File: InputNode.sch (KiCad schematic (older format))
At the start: 3 parts, among them J6 Conn_01x04_Female

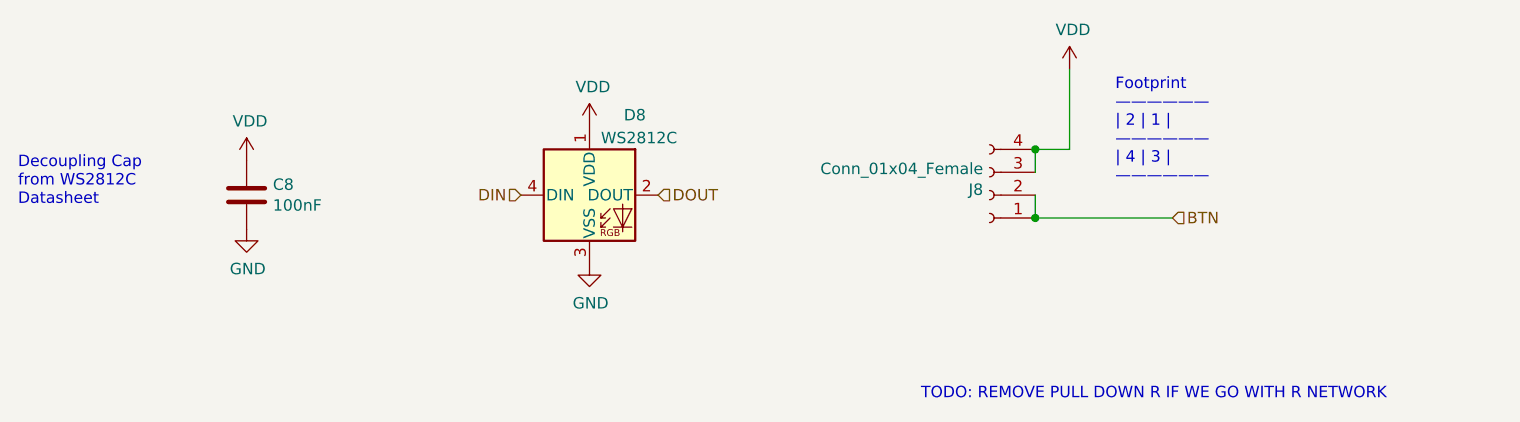
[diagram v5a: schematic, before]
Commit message: finished first pass at routing
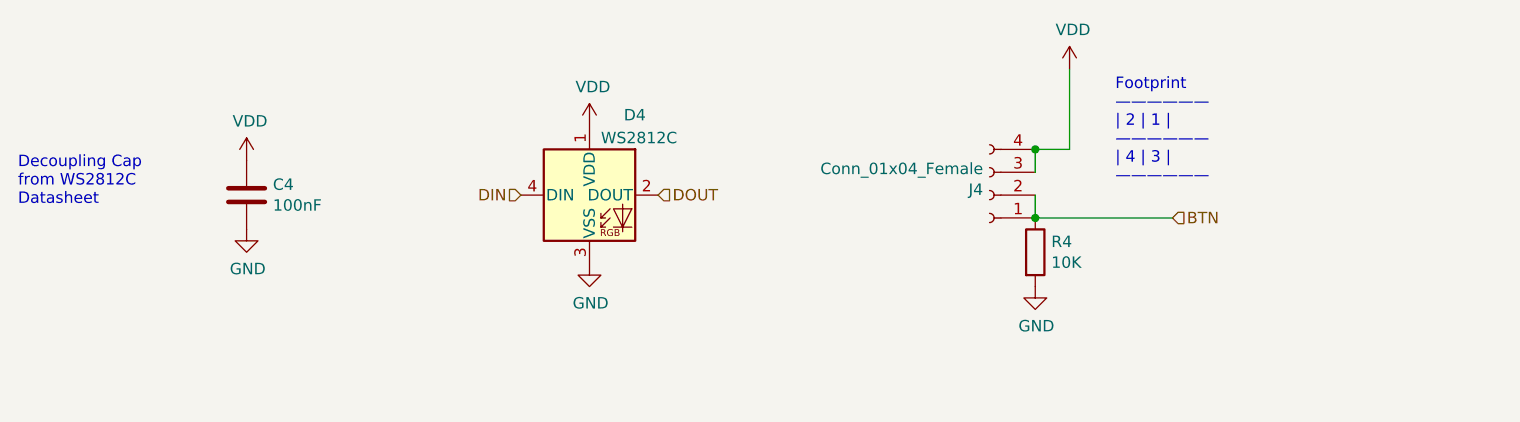
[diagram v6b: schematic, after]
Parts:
- added R1: 10K, Resistor_SMD:R_0805_2012Metric_Pad1.20x1.40mm_HandSolder, symbol Device:R
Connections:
- net BTN: now also R1.1
- net GND: now also R1.2
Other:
- note removed: "TODO: REMOVE PULL DOWN R IF WE GO WITH R NETWORK"
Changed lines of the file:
@@
 $Descr A4 11693 8268
 encoding utf-8
-Sheet 9 9
+Sheet 5 9
 Title ""
 Date ""
@@
 AR Path="/61554F98/61493950" Ref="#PWR049"  Part="1"
 AR Path="/61555D68/61493950" Ref="#PWR?"  Part="1"
-F 0 "#PWR049" H 7700 3100 50  0001 C CNN
+F 0 "#PWR025" H 7700 3100 50  0001 C CNN
 F 1 "VDD" H 7715 3423 50  0000 C CNN
 F 2 "" H 7700 3250 50  0001 C CNN
@@
 AR Path="/61554F98/61493958" Ref="D8"  Part="1"
 AR Path="/61555D68/61493958" Ref="D?"  Part="1"
-F 0 "D8" H 5750 4150 50  0000 L CNN
+F 0 "D4" H 5750 4150 50  0000 L CNN
 F 1 "WS2812C" H 5650 4050 50  0000 L CNN
 F 2 "LED_SMD:LED_WS2812B_PLCC4_5.0x5.0mm_P3.2mm" H 5650 3500 50  0001 L TNN
@@
 AR Path="/61554F98/61495684" Ref="#PWR048"  Part="1"
 AR Path="/61555D68/61495684" Ref="#PWR?"  Part="1"
-F 0 "#PWR048" H 5600 3850 50  0001 C CNN
+F 0 "#PWR024" H 5600 3850 50  0001 C CNN
 F 1 "GND" H 5605 3927 50  0000 C CNN
 F 2 "" H 5600 4100 50  0001 C CNN
@@
 AR Path="/61554F98/61495D51" Ref="#PWR047"  Part="1"
 AR Path="/61555D68/61495D51" Ref="#PWR?"  Part="1"
-F 0 "#PWR047" H 5600 3350 50  0001 C CNN
+F 0 "#PWR023" H 5600 3350 50  0001 C CNN
 F 1 "VDD" H 5615 3673 50  0000 C CNN
 F 2 "" H 5600 3500 50  0001 C CNN
@@
 AR Path="/61554F98/614A34FE" Ref="C8"  Part="1"
 AR Path="/61555D68/614A34FE" Ref="C?"  Part="1"
-F 0 "C8" H 4215 3846 50  0000 L CNN
+F 0 "C4" H 4215 3846 50  0000 L CNN
 F 1 "100nF" H 4215 3755 50  0000 L CNN
 F 2 "Capacitor_SMD:C_0805_2012Metric_Pad1.15x1.40mm_HandSolder" H 4138 3650 50  0001 C CNN
@@
 AR Path="/61554F98/614A4287" Ref="#PWR046"  Part="1"
 AR Path="/61555D68/614A4287" Ref="#PWR?"  Part="1"
-F 0 "#PWR046" H 4100 3700 50  0001 C CNN
+F 0 "#PWR022" H 4100 3700 50  0001 C CNN
 F 1 "GND" H 4105 3777 50  0000 C CNN
 F 2 "" H 4100 3950 50  0001 C CNN
@@
 AR Path="/61554F98/614A4795" Ref="#PWR045"  Part="1"
 AR Path="/61555D68/614A4795" Ref="#PWR?"  Part="1"
-F 0 "#PWR045" H 4100 3500 50  0001 C CNN
+F 0 "#PWR021" H 4100 3500 50  0001 C CNN
 F 1 "VDD" H 4115 3823 50  0000 C CNN
 F 2 "" H 4100 3650 50  0001 C CNN
@@
 AR Path="/61554F92/6156DDAC" Ref="J7"  Part="1"
 AR Path="/61554F98/6156DDAC" Ref="J8"  Part="1"
-F 0 "J8" H 7378 3776 50  0000 L CNN
+F 0 "J4" H 7378 3776 50  0000 L CNN
 F 1 "Conn_01x04_Female" H 7378 3685 50  0000 L CNN
 F 2 "Connector_PinSocket_2.54mm:PinSocket_2x02_P2.54mm_Vertical" H 7350 3800 50  0001 C CNN
@@
 Connection ~ 7550 3600
 Connection ~ 7550 3900
-Text Notes 7050 4700 0    50   ~ 0
-TODO: REMOVE PULL DOWN R IF WE GO WITH R NETWORK
 Wire Wire Line
 	7550 3900 8150 3900
+$Comp
+L Device:R R1
+U 1 1 6160802E
+P 7550 4050
+AR Path="/6149038E/6160802E" Ref="R1"  Part="1"
+AR Path="/61554F98/6160802E" Ref="R8"  Part="1"
+AR Path="/614A08BA/6160802E" Ref="R2"  Part="1"
+AR Path="/61551931/6160802E" Ref="R3"  Part="1"
+AR Path="/6155214B/6160802E" Ref="R4"  Part="1"
+AR Path="/61552612/6160802E" Ref="R5"  Part="1"
+AR Path="/61552B2D/6160802E" Ref="R6"  Part="1"
+AR Path="/61554F92/6160802E" Ref="R7"  Part="1"
+F 0 "R4" H 7620 4096 50  0000 L CNN
+F 1 "10K" H 7620 4005 50  0000 L CNN
+F 2 "Resistor_SMD:R_0805_2012Metric_Pad1.20x1.40mm_HandSolder" V 7480 4050 50  0001 C CNN
+F 3 "~" H 7550 4050 50  0001 C CNN
+	1    7550 4050
+	1    0    0    -1
+$EndComp
+$Comp
+L power:GND #PWR?
+U 1 1 61608726
+P 7550 4200
+AR Path="/61608726" Ref="#PWR?"  Part="1"
+AR Path="/6149038E/61608726" Ref="#PWR0103"  Part="1"
+AR Path="/614A08BA/61608726" Ref="#PWR0104"  Part="1"
+AR Path="/61551931/61608726" Ref="#PWR0105"  Part="1"
+AR Path="/6155214B/61608726" Ref="#PWR0106"  Part="1"
+AR Path="/61552612/61608726" Ref="#PWR0107"  Part="1"
+AR Path="/61552B2D/61608726" Ref="#PWR0108"  Part="1"
+AR Path="/61553054/61608726" Ref="#PWR?"  Part="1"
+AR Path="/61554F92/61608726" Ref="#PWR0109"  Part="1"
+AR Path="/61554F98/61608726" Ref="#PWR0110"  Part="1"
+AR Path="/61555D68/61608726" Ref="#PWR?"  Part="1"
+F 0 "#PWR0106" H 7550 3950 50  0001 C CNN
+F 1 "GND" H 7555 4027 50  0000 C CNN
+F 2 "" H 7550 4200 50  0001 C CNN
+F 3 "" H 7550 4200 50  0001 C CNN
+	1    7550 4200
+	1    0    0    -1
+$EndComp
 $EndSCHEMATC

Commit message: updated with todo for routing around screws
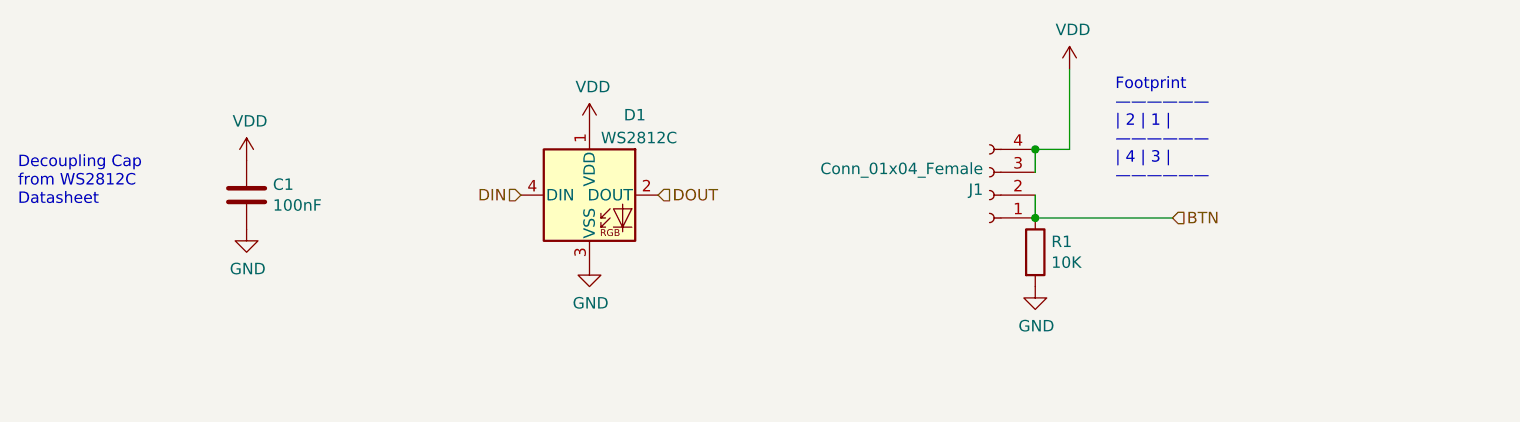
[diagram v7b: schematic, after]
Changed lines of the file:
@@
 $Descr A4 11693 8268
 encoding utf-8
-Sheet 5 9
+Sheet 2 9
 Title ""
 Date ""
@@
 AR Path="/61554F98/61493950" Ref="#PWR049"  Part="1"
 AR Path="/61555D68/61493950" Ref="#PWR?"  Part="1"
-F 0 "#PWR025" H 7700 3100 50  0001 C CNN
+F 0 "#PWR05" H 7700 3100 50  0001 C CNN
 F 1 "VDD" H 7715 3423 50  0000 C CNN
 F 2 "" H 7700 3250 50  0001 C CNN
@@
 AR Path="/61554F98/61493958" Ref="D8"  Part="1"
 AR Path="/61555D68/61493958" Ref="D?"  Part="1"
-F 0 "D4" H 5750 4150 50  0000 L CNN
+F 0 "D1" H 5750 4150 50  0000 L CNN
 F 1 "WS2812C" H 5650 4050 50  0000 L CNN
 F 2 "LED_SMD:LED_WS2812B_PLCC4_5.0x5.0mm_P3.2mm" H 5650 3500 50  0001 L TNN
@@
 AR Path="/61554F98/61495684" Ref="#PWR048"  Part="1"
 AR Path="/61555D68/61495684" Ref="#PWR?"  Part="1"
-F 0 "#PWR024" H 5600 3850 50  0001 C CNN
+F 0 "#PWR04" H 5600 3850 50  0001 C CNN
 F 1 "GND" H 5605 3927 50  0000 C CNN
 F 2 "" H 5600 4100 50  0001 C CNN
@@
 AR Path="/61554F98/61495D51" Ref="#PWR047"  Part="1"
 AR Path="/61555D68/61495D51" Ref="#PWR?"  Part="1"
-F 0 "#PWR023" H 5600 3350 50  0001 C CNN
+F 0 "#PWR03" H 5600 3350 50  0001 C CNN
 F 1 "VDD" H 5615 3673 50  0000 C CNN
 F 2 "" H 5600 3500 50  0001 C CNN
@@
 AR Path="/61554F98/614A34FE" Ref="C8"  Part="1"
 AR Path="/61555D68/614A34FE" Ref="C?"  Part="1"
-F 0 "C4" H 4215 3846 50  0000 L CNN
+F 0 "C1" H 4215 3846 50  0000 L CNN
 F 1 "100nF" H 4215 3755 50  0000 L CNN
 F 2 "Capacitor_SMD:C_0805_2012Metric_Pad1.15x1.40mm_HandSolder" H 4138 3650 50  0001 C CNN
@@
 AR Path="/61554F98/614A4287" Ref="#PWR046"  Part="1"
 AR Path="/61555D68/614A4287" Ref="#PWR?"  Part="1"
-F 0 "#PWR022" H 4100 3700 50  0001 C CNN
+F 0 "#PWR08" H 4100 3700 50  0001 C CNN
 F 1 "GND" H 4105 3777 50  0000 C CNN
 F 2 "" H 4100 3950 50  0001 C CNN
@@
 AR Path="/61554F98/614A4795" Ref="#PWR045"  Part="1"
 AR Path="/61555D68/614A4795" Ref="#PWR?"  Part="1"
-F 0 "#PWR021" H 4100 3500 50  0001 C CNN
+F 0 "#PWR07" H 4100 3500 50  0001 C CNN
 F 1 "VDD" H 4115 3823 50  0000 C CNN
 F 2 "" H 4100 3650 50  0001 C CNN
@@
 AR Path="/61554F92/6156DDAC" Ref="J7"  Part="1"
 AR Path="/61554F98/6156DDAC" Ref="J8"  Part="1"
-F 0 "J4" H 7378 3776 50  0000 L CNN
+F 0 "J1" H 7378 3776 50  0000 L CNN
 F 1 "Conn_01x04_Female" H 7378 3685 50  0000 L CNN
 F 2 "Connector_PinSocket_2.54mm:PinSocket_2x02_P2.54mm_Vertical" H 7350 3800 50  0001 C CNN
@@
 AR Path="/61552B2D/6160802E" Ref="R6"  Part="1"
 AR Path="/61554F92/6160802E" Ref="R7"  Part="1"
-F 0 "R4" H 7620 4096 50  0000 L CNN
+F 0 "R1" H 7620 4096 50  0000 L CNN
 F 1 "10K" H 7620 4005 50  0000 L CNN
 F 2 "Resistor_SMD:R_0805_2012Metric_Pad1.20x1.40mm_HandSolder" V 7480 4050 50  0001 C CNN
@@
 AR Path="/61554F98/61608726" Ref="#PWR0110"  Part="1"
 AR Path="/61555D68/61608726" Ref="#PWR?"  Part="1"
-F 0 "#PWR0106" H 7550 3950 50  0001 C CNN
+F 0 "#PWR0103" H 7550 3950 50  0001 C CNN
 F 1 "GND" H 7555 4027 50  0000 C CNN
 F 2 "" H 7550 4200 50  0001 C CNN

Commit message: fixed added cap for mux and fixed drc errors
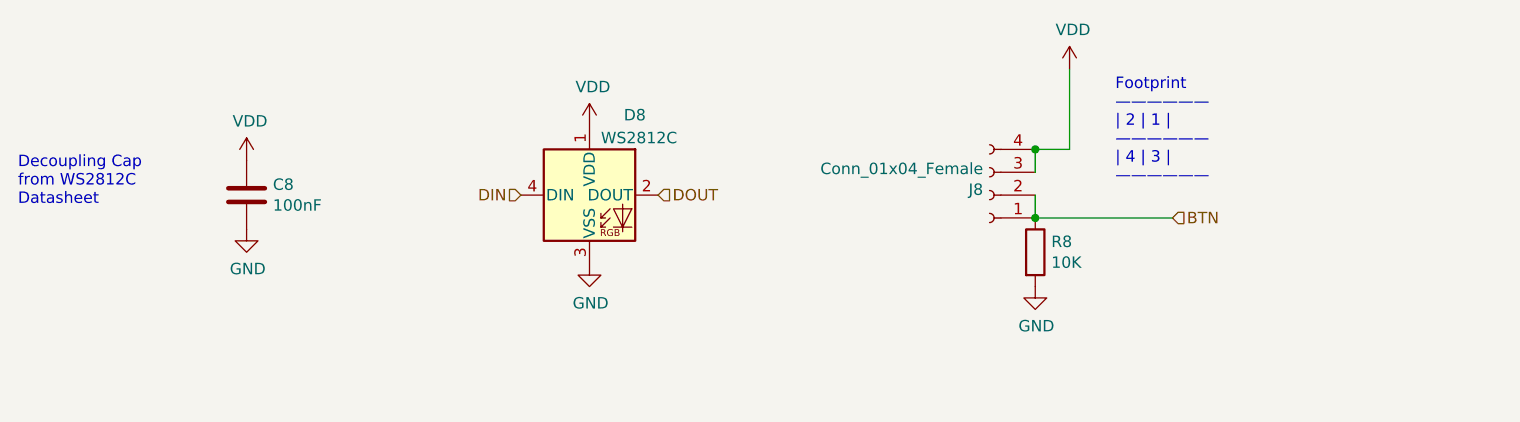
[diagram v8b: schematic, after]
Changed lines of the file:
@@
 AR Path="/61554F98/61493950" Ref="#PWR049"  Part="1"
 AR Path="/61555D68/61493950" Ref="#PWR?"  Part="1"
-F 0 "#PWR05" H 7700 3100 50  0001 C CNN
+F 0 "#PWR049" H 7700 3100 50  0001 C CNN
 F 1 "VDD" H 7715 3423 50  0000 C CNN
 F 2 "" H 7700 3250 50  0001 C CNN
@@
 AR Path="/61554F98/61493958" Ref="D8"  Part="1"
 AR Path="/61555D68/61493958" Ref="D?"  Part="1"
-F 0 "D1" H 5750 4150 50  0000 L CNN
+F 0 "D8" H 5750 4150 50  0000 L CNN
 F 1 "WS2812C" H 5650 4050 50  0000 L CNN
 F 2 "LED_SMD:LED_WS2812B_PLCC4_5.0x5.0mm_P3.2mm" H 5650 3500 50  0001 L TNN
@@
 AR Path="/61554F98/61495684" Ref="#PWR048"  Part="1"
 AR Path="/61555D68/61495684" Ref="#PWR?"  Part="1"
-F 0 "#PWR04" H 5600 3850 50  0001 C CNN
+F 0 "#PWR048" H 5600 3850 50  0001 C CNN
 F 1 "GND" H 5605 3927 50  0000 C CNN
 F 2 "" H 5600 4100 50  0001 C CNN
@@
 AR Path="/61554F98/61495D51" Ref="#PWR047"  Part="1"
 AR Path="/61555D68/61495D51" Ref="#PWR?"  Part="1"
-F 0 "#PWR03" H 5600 3350 50  0001 C CNN
+F 0 "#PWR047" H 5600 3350 50  0001 C CNN
 F 1 "VDD" H 5615 3673 50  0000 C CNN
 F 2 "" H 5600 3500 50  0001 C CNN
@@
 AR Path="/61554F98/614A34FE" Ref="C8"  Part="1"
 AR Path="/61555D68/614A34FE" Ref="C?"  Part="1"
-F 0 "C1" H 4215 3846 50  0000 L CNN
+F 0 "C8" H 4215 3846 50  0000 L CNN
 F 1 "100nF" H 4215 3755 50  0000 L CNN
 F 2 "Capacitor_SMD:C_0805_2012Metric_Pad1.15x1.40mm_HandSolder" H 4138 3650 50  0001 C CNN
@@
 AR Path="/61554F98/614A4287" Ref="#PWR046"  Part="1"
 AR Path="/61555D68/614A4287" Ref="#PWR?"  Part="1"
-F 0 "#PWR08" H 4100 3700 50  0001 C CNN
+F 0 "#PWR046" H 4100 3700 50  0001 C CNN
 F 1 "GND" H 4105 3777 50  0000 C CNN
 F 2 "" H 4100 3950 50  0001 C CNN
@@
 AR Path="/61554F98/614A4795" Ref="#PWR045"  Part="1"
 AR Path="/61555D68/614A4795" Ref="#PWR?"  Part="1"
-F 0 "#PWR07" H 4100 3500 50  0001 C CNN
+F 0 "#PWR045" H 4100 3500 50  0001 C CNN
 F 1 "VDD" H 4115 3823 50  0000 C CNN
 F 2 "" H 4100 3650 50  0001 C CNN
@@
 AR Path="/61554F92/6156DDAC" Ref="J7"  Part="1"
 AR Path="/61554F98/6156DDAC" Ref="J8"  Part="1"
-F 0 "J1" H 7378 3776 50  0000 L CNN
+F 0 "J8" H 7378 3776 50  0000 L CNN
 F 1 "Conn_01x04_Female" H 7378 3685 50  0000 L CNN
 F 2 "Connector_PinSocket_2.54mm:PinSocket_2x02_P2.54mm_Vertical" H 7350 3800 50  0001 C CNN
@@
 AR Path="/61552B2D/6160802E" Ref="R6"  Part="1"
 AR Path="/61554F92/6160802E" Ref="R7"  Part="1"
-F 0 "R1" H 7620 4096 50  0000 L CNN
+F 0 "R8" H 7620 4096 50  0000 L CNN
 F 1 "10K" H 7620 4005 50  0000 L CNN
 F 2 "Resistor_SMD:R_0805_2012Metric_Pad1.20x1.40mm_HandSolder" V 7480 4050 50  0001 C CNN
@@
 AR Path="/61554F98/61608726" Ref="#PWR0110"  Part="1"
 AR Path="/61555D68/61608726" Ref="#PWR?"  Part="1"
-F 0 "#PWR0103" H 7550 3950 50  0001 C CNN
+F 0 "#PWR0110" H 7550 3950 50  0001 C CNN
 F 1 "GND" H 7555 4027 50  0000 C CNN
 F 2 "" H 7550 4200 50  0001 C CNN
